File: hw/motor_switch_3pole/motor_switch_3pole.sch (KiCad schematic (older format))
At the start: 24 parts, among them J1 CONN_3X1, J2 CONN_2X1, J3 CONN_6X1, Q1 BSS138, Q2 BSS138

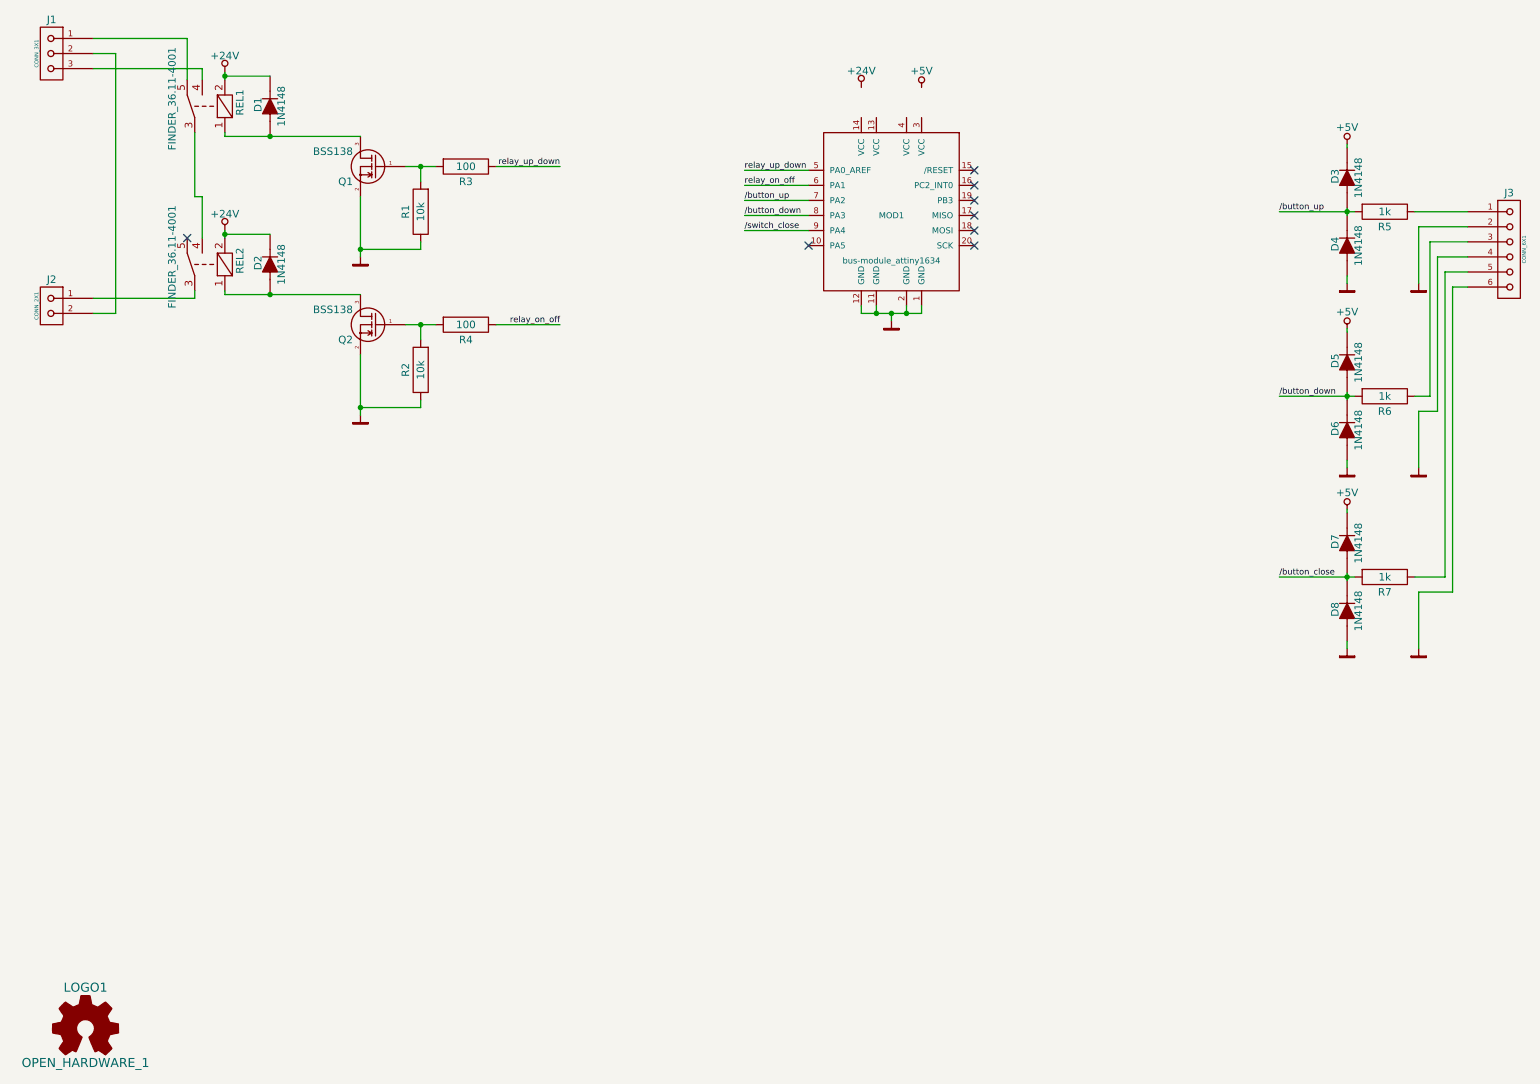
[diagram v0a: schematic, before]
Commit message: changed to SMD components
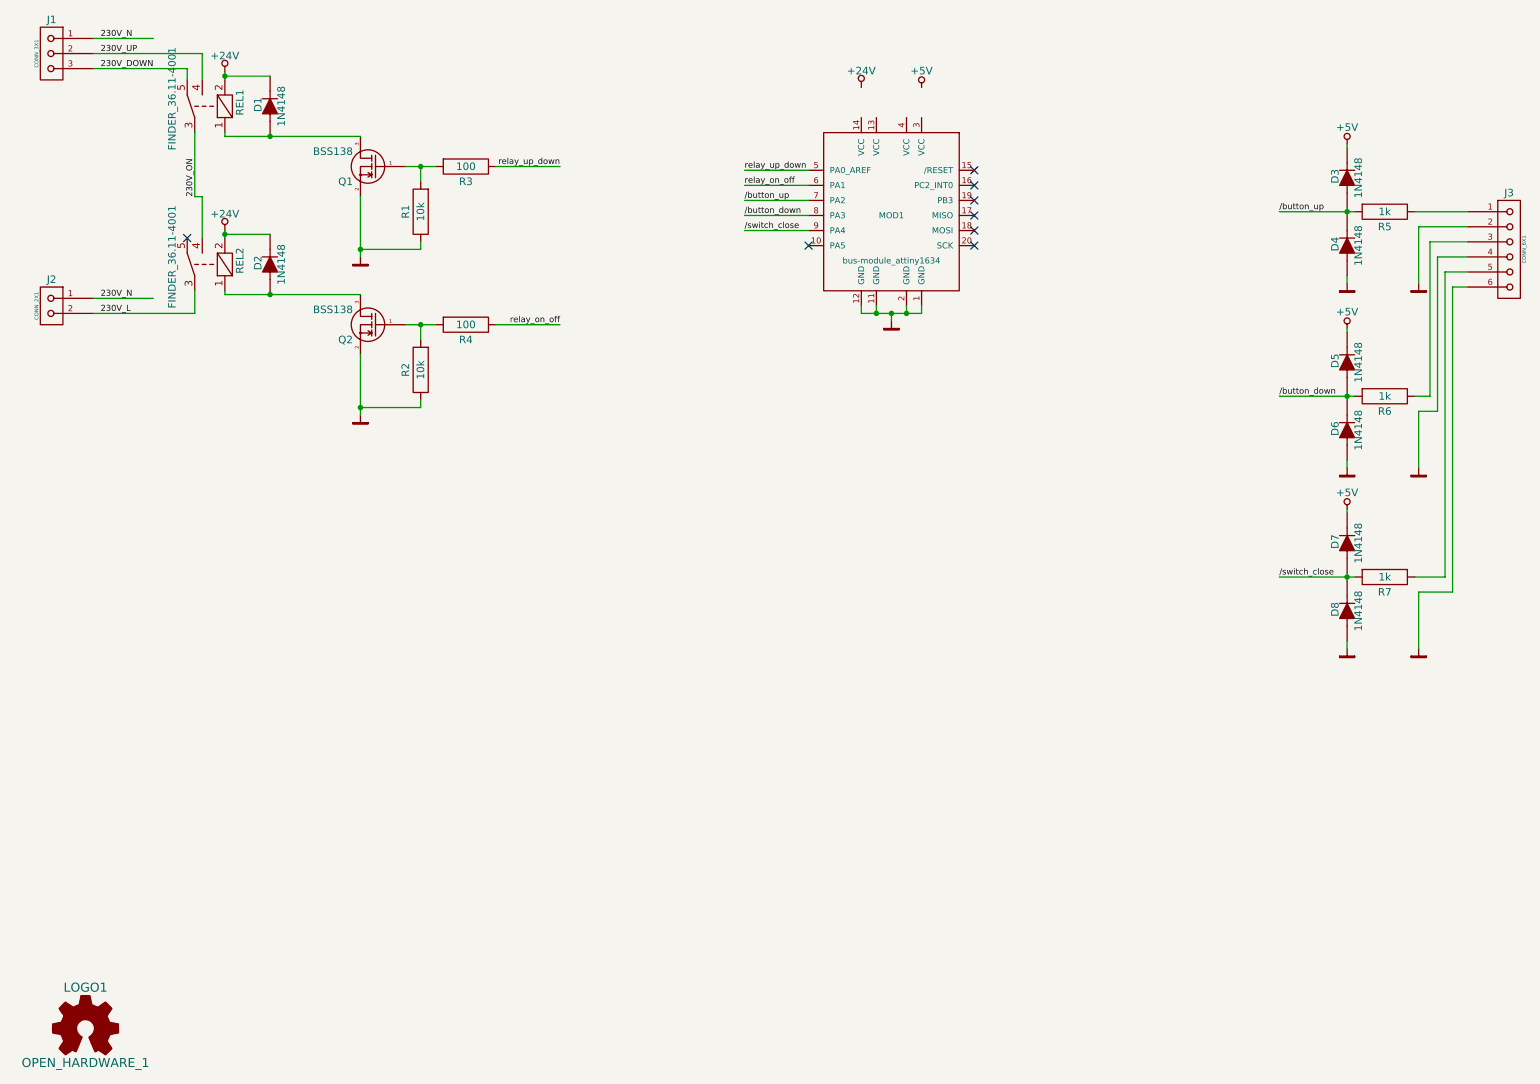
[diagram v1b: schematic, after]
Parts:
- D1, D2, D3, D4, D5, D6, D7, D8: footprint Diode_THT:D_RM2.54mm -> Diode_SMD:D_SOD323
- R1, R2, R3, R4, R5, R6, R7: footprint Resistor:R_RM2.54mm -> Resistor:R_0805
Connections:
- net /button_close is gone; now on net /switch_close: D7.1 (A), D8.2 (C), R7.1
- net 230V_ON: now reaches REL1.3, REL2.4
- net 230V_DOWN: now reaches J1.3
- net 230V_DOWN: now also REL1.5; no longer REL1.4
- net 230V_N: now reaches J1.1
- net 230V_N: now also J2.1; no longer REL1.5
- net 230V_L: now reaches REL2.3
- net 230V_L: now also J2.2; no longer J2.1
- net 230V_UP: now reaches J1.2
- net 230V_UP: now also REL1.4; no longer J2.2
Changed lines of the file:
@@
 F 0 "D1" H 2210 1305 50  0000 C CNN
 F 1 "1N4148" H 2200 1150 50  0000 C CNN
-F 2 "Diode_THT:D_RM2.54mm" H 2200 1225 60  0001 C CNN
+F 2 "Diode_SMD:D_SOD323" H 2200 1225 60  0001 C CNN
 F 3 "" H 2200 1225 60  0000 C CNN
 	1    2200 1225
@@
 F 0 "D2" H 2210 2355 50  0000 C CNN
 F 1 "1N4148" H 2200 2200 50  0000 C CNN
-F 2 "Diode_THT:D_RM2.54mm" H 2200 2275 60  0001 C CNN
+F 2 "Diode_SMD:D_SOD323" H 2200 2275 60  0001 C CNN
 F 3 "" H 2200 2275 60  0000 C CNN
 	1    2200 2275
@@
 F 0 "R3" H 3500 1525 50  0000 C CNN
 F 1 "100" H 3500 1625 50  0000 C CNN
-F 2 "Resistor:R_RM2.54mm" H 3500 1625 60  0001 C CNN
+F 2 "Resistor:R_0805" H 3500 1625 60  0001 C CNN
 F 3 "" H 3500 1625 60  0000 C CNN
 	1    3500 1625
@@
 F 0 "R1" H 3200 1825 50  0000 C CNN
 F 1 "10k" H 3200 1925 50  0000 C CNN
-F 2 "Resistor:R_RM2.54mm" H 3200 1925 60  0001 C CNN
+F 2 "Resistor:R_0805" H 3200 1925 60  0001 C CNN
 F 3 "" H 3200 1925 60  0000 C CNN
 	1    3200 1925
@@
 F 0 "R2" H 3200 2875 50  0000 C CNN
 F 1 "10k" H 3200 2975 50  0000 C CNN
-F 2 "Resistor:R_RM2.54mm" H 3200 2975 60  0001 C CNN
+F 2 "Resistor:R_0805" H 3200 2975 60  0001 C CNN
 F 3 "" H 3200 2975 60  0000 C CNN
 	1    3200 2975
@@
 F 0 "R4" H 3500 2575 50  0000 C CNN
 F 1 "100" H 3500 2675 50  0000 C CNN
-F 2 "Resistor:R_RM2.54mm" H 3500 2675 60  0001 C CNN
+F 2 "Resistor:R_0805" H 3500 2675 60  0001 C CNN
 F 3 "" H 3500 2675 60  0000 C CNN
 	1    3500 2675
@@
 	1900 2475 1900 2450
 Wire Wire Line
-	1025 875  1175 875
-Wire Wire Line
-	1175 2600 1025 2600
-Wire Wire Line
-	1025 2500 1700 2500
-Wire Wire Line
-	1700 2500 1700 2450
-Wire Wire Line
-	1650 1050 1650 775
-Wire Wire Line
-	1650 775  1025 775
-Wire Wire Line
-	1750 1050 1750 975
-Wire Wire Line
-	1750 975  1025 975
-Wire Wire Line
 	2800 2225 2800 1825
 Connection ~ 2200 1425
@@
 	3200 2175 2800 2175
 Connection ~ 2800 2175
-Wire Wire Line
-	1175 875  1175 2600
 Wire Wire Line
 	1750 2100 1750 1825
@@
 F 0 "D3" H 9360 1780 50  0000 C CNN
 F 1 "1N4148" H 9350 1625 50  0000 C CNN
-F 2 "Diode_THT:D_RM2.54mm" H 9350 1700 60  0001 C CNN
+F 2 "Diode_SMD:D_SOD323" H 9350 1700 60  0001 C CNN
 F 3 "" H 9350 1700 60  0000 C CNN
 	1    9350 1700
@@
 F 0 "D4" H 9360 2230 50  0000 C CNN
 F 1 "1N4148" H 9350 2075 50  0000 C CNN
-F 2 "Diode_THT:D_RM2.54mm" H 9350 2150 60  0001 C CNN
+F 2 "Diode_SMD:D_SOD323" H 9350 2150 60  0001 C CNN
 F 3 "" H 9350 2150 60  0000 C CNN
 	1    9350 2150
@@
 F 0 "R5" H 9600 1825 50  0000 C CNN
 F 1 "1k" H 9600 1925 50  0000 C CNN
-F 2 "Resistor:R_RM2.54mm" H 9600 1925 60  0001 C CNN
+F 2 "Resistor:R_0805" H 9600 1925 60  0001 C CNN
 F 3 "" H 9600 1925 60  0000 C CNN
 	1    9600 1925
@@
 F 0 "D5" H 9360 3005 50  0000 C CNN
 F 1 "1N4148" H 9350 2850 50  0000 C CNN
-F 2 "Diode_THT:D_RM2.54mm" H 9350 2925 60  0001 C CNN
+F 2 "Diode_SMD:D_SOD323" H 9350 2925 60  0001 C CNN
 F 3 "" H 9350 2925 60  0000 C CNN
 	1    9350 2925
@@
 F 0 "D6" H 9360 3455 50  0000 C CNN
 F 1 "1N4148" H 9350 3300 50  0000 C CNN
-F 2 "Diode_THT:D_RM2.54mm" H 9350 3375 60  0001 C CNN
+F 2 "Diode_SMD:D_SOD323" H 9350 3375 60  0001 C CNN
 F 3 "" H 9350 3375 60  0000 C CNN
 	1    9350 3375
@@
 F 0 "R6" H 9600 3050 50  0000 C CNN
 F 1 "1k" H 9600 3150 50  0000 C CNN
-F 2 "Resistor:R_RM2.54mm" H 9600 3150 60  0001 C CNN
+F 2 "Resistor:R_0805" H 9600 3150 60  0001 C CNN
 F 3 "" H 9600 3150 60  0000 C CNN
 	1    9600 3150
@@
 F 0 "D7" H 9360 4205 50  0000 C CNN
 F 1 "1N4148" H 9350 4050 50  0000 C CNN
-F 2 "Diode_THT:D_RM2.54mm" H 9350 4125 60  0001 C CNN
+F 2 "Diode_SMD:D_SOD323" H 9350 4125 60  0001 C CNN
 F 3 "" H 9350 4125 60  0000 C CNN
 	1    9350 4125
@@
 F 0 "D8" H 9360 4655 50  0000 C CNN
 F 1 "1N4148" H 9350 4500 50  0000 C CNN
-F 2 "Diode_THT:D_RM2.54mm" H 9350 4575 60  0001 C CNN
+F 2 "Diode_SMD:D_SOD323" H 9350 4575 60  0001 C CNN
 F 3 "" H 9350 4575 60  0000 C CNN
 	1    9350 4575
@@
 F 0 "R7" H 9600 4250 50  0000 C CNN
 F 1 "1k" H 9600 4350 50  0000 C CNN
-F 2 "Resistor:R_RM2.54mm" H 9600 4350 60  0001 C CNN
+F 2 "Resistor:R_0805" H 9600 4350 60  0001 C CNN
 F 3 "" H 9600 4350 60  0000 C CNN
 	1    9600 4350
@@
 Connection ~ 9350 4350
 Text Label 8900 4350 0    40   ~ 0
-/button_close
+/switch_close
 $Comp
 L +5V #PWR012
@@
 	-1   0    0    -1
 $EndComp
+Text Label 1075 875  0    40   ~ 0
+230V_UP
+Text Label 1075 975  0    40   ~ 0
+230V_DOWN
+Text Label 1700 1825 1    40   ~ 0
+230V_ON
+Text Label 1075 775  0    40   ~ 0
+230V_N
+Text Label 1075 2600 0    40   ~ 0
+230V_L
+Wire Wire Line
+	1650 1050 1650 975
+Wire Wire Line
+	1650 975  1025 975
+Wire Wire Line
+	1025 875  1750 875
+Wire Wire Line
+	1750 875  1750 1050
+Wire Wire Line
+	1025 2600 1700 2600
+Wire Wire Line
+	1700 2600 1700 2450
+Wire Wire Line
+	1025 2500 1425 2500
+Wire Wire Line
+	1025 775  1425 775
+Text Label 1075 2500 0    40   ~ 0
+230V_N
 $EndSCHEMATC

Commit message: motor control 3pole layouted and ready for review
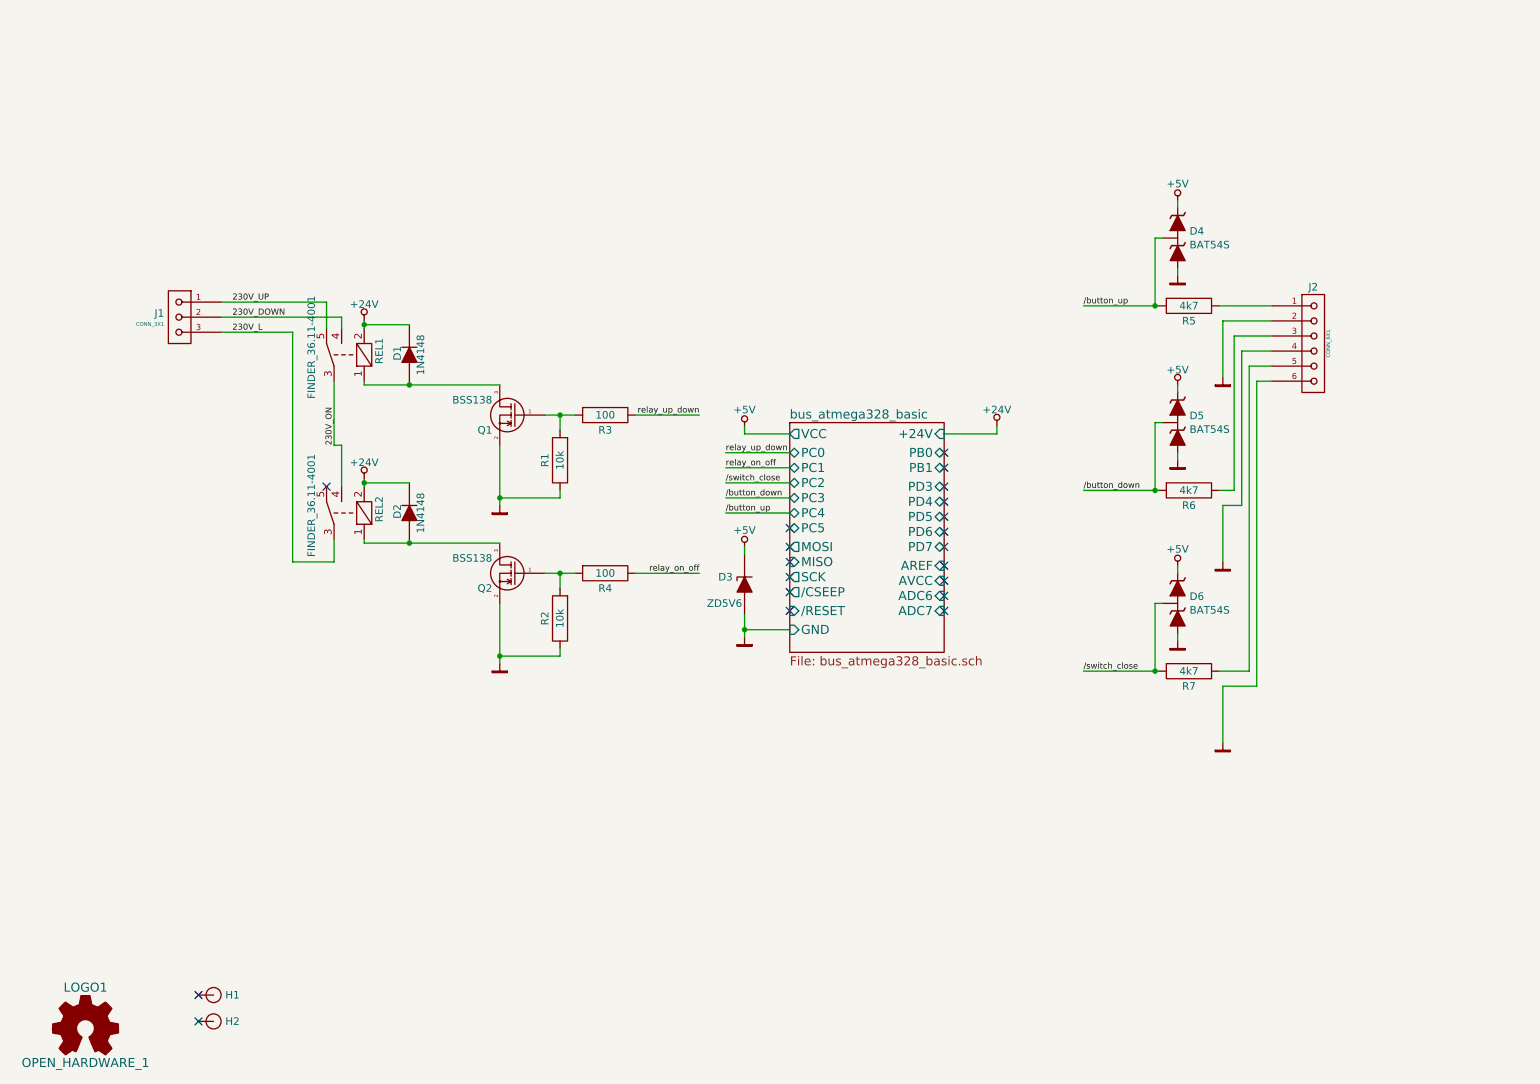
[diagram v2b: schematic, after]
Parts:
- removed D3, D4, D5, D6, D7, D8: 1N4148, Diode_SMD:D_SOD323, symbol D
- removed J2: CONN_2X1, Connector_Miscelleaneus:CLAMP_5,08mm_2pole_stackable, symbol CONN_2X1
- removed MOD1: bus-module_attiny1634, Modules:bus-module_attiny1634, symbol bus-module_attiny1634
- added D3: ZD5V6, Diode_SMD:D_MINIMELF, symbol ZD
- added D4, D5, D6: BAT54S, Housings_SOT:SOT23-3, symbol BAT54S
- added H1, H2: HOLE, Mechanical:HOLE_2.5mm_wo_Copper, symbol HOLE
- J1: footprint Connector_Miscelleaneus:CLAMP_5,08mm_3pole_stackable -> Connector_WAGO:WAGO_2081-1123
- J2: renamed from J3; footprint Connector_Miscelleaneus:WAGO_233-6 -> Connector_WAGO:WAGO_233-6
- R5, R6, R7: value 1k -> 4k7
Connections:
- net 230V_N is gone; now on net 230V_UP: J1.1
- net +5V: now also D3.2 (C), D4.2, D5.2, D6.2
- net /button_down: now also D5.3
- net /button_up: now also D4.3
- net /switch_close: now also D6.3
- net 230V_DOWN: now also J1.2, REL1.4; no longer J1.3, REL1.5
- net 230V_L: now also J1.3
- net 230V_UP: now also REL1.5; no longer J1.2, REL1.4
- net GND: now also D3.1 (A), D4.1, D5.1, D6.1
- no-connect marks 8 -> 20
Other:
- moved on the sheet: D1, D2, J2, Q1, Q2, R1, R2, R3, R4, R5, R6, R7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

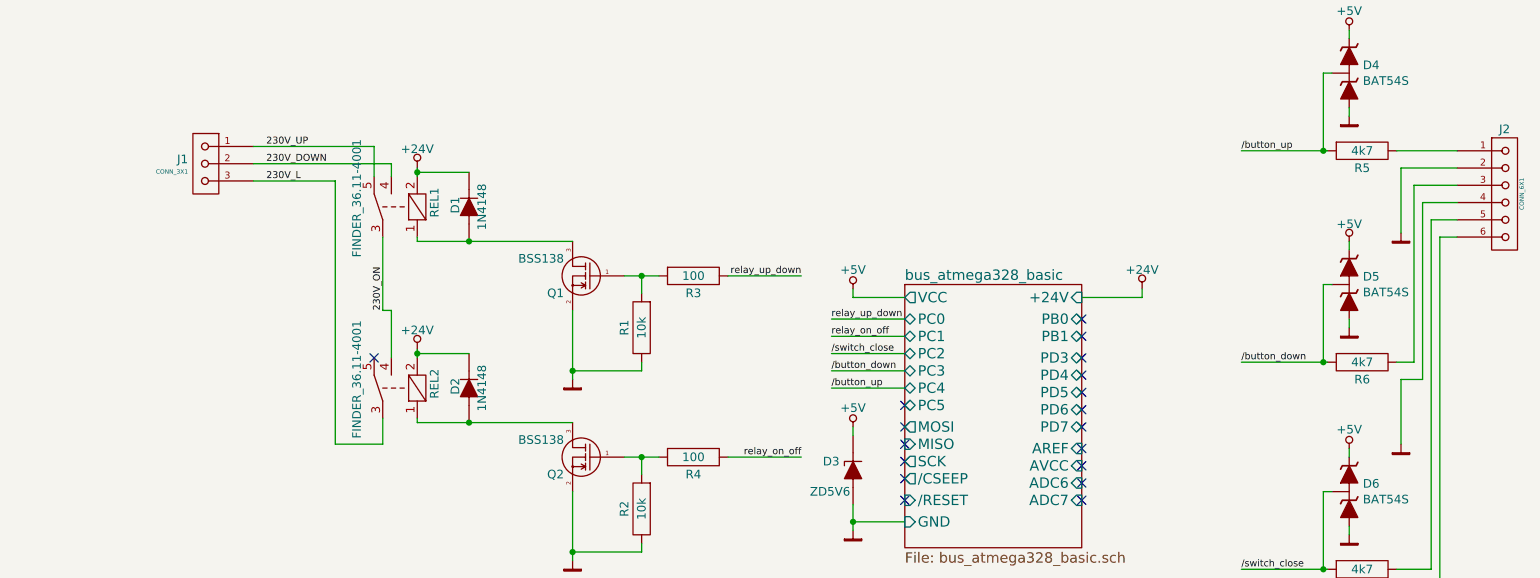
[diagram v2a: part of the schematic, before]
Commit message: Final revision 1 files of motor_switch_3pole added. Prototype PCBs of this revision have been ordered
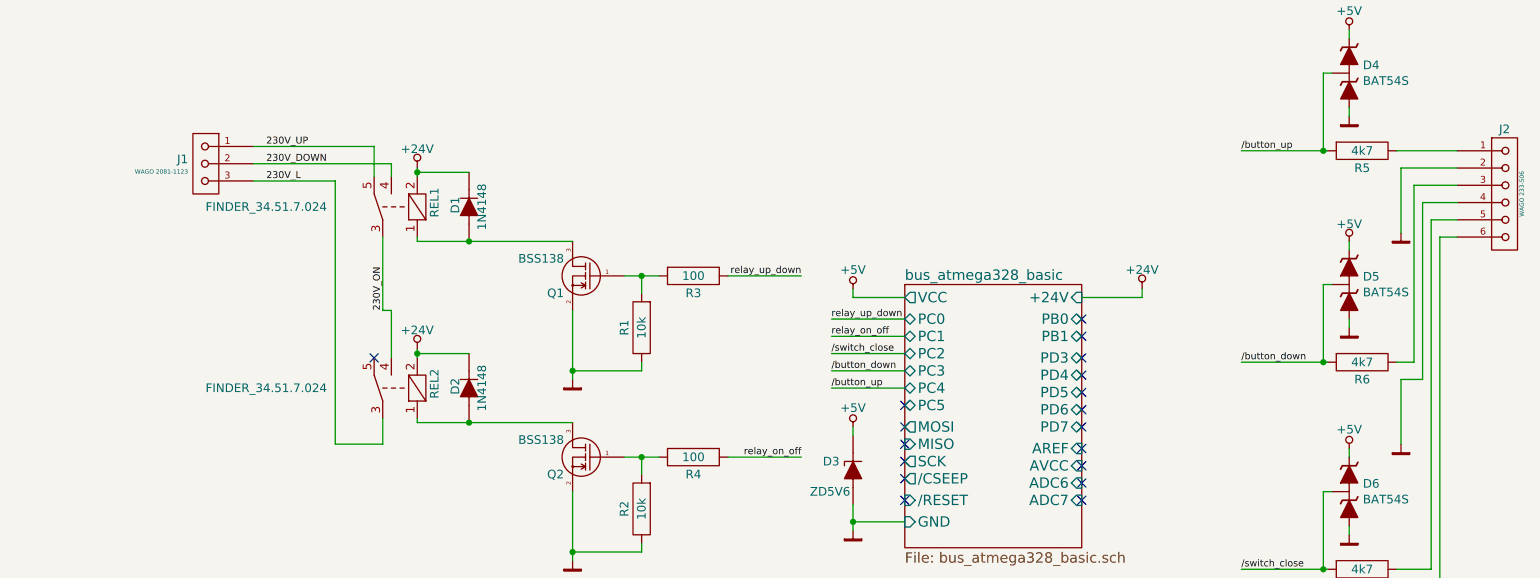
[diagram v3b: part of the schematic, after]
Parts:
- J1: value CONN_3X1 -> WAGO 2081-1123
- J2: value CONN_6X1 -> WAGO 233-506
- REL1, REL2: value FINDER_36.11-4001 -> FINDER_34.51.7.024
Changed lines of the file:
@@
 Sheet 1 2
 Title "motor switch 3pole"
-Date "2016-08-10"
+Date "2016-09-06"
 Rev "1"
 Comp "koewiba"
@@
 P 2825 2875
 F 0 "REL1" H 2850 2775 50  0000 C CNN
-F 1 "FINDER_36.11-4001" H 2875 3225 50  0000 C CNN
+F 1 "FINDER_34.51.7.024" V 2825 3750 50  0000 C CNN
 F 2 "Relay:finder_34.51_1xUM" H 2825 2875 60  0001 C CNN
 F 3 "" H 2825 2875 60  0000 C CNN
@@
 P 2825 3925
 F 0 "REL2" H 2850 3825 50  0000 C CNN
-F 1 "FINDER_36.11-4001" H 2875 4275 50  0000 C CNN
+F 1 "FINDER_34.51.7.024" V 2825 4800 50  0000 C CNN
 F 2 "Relay:finder_34.51_1xUM" H 2825 3925 60  0001 C CNN
 F 3 "" H 2825 3925 60  0000 C CNN
@@
 P 9050 2800
 F 0 "J2" H 9125 3175 50  0000 C CNN
-F 1 "CONN_6X1" V 9225 2800 25  0000 C CNN
+F 1 "WAGO 233-506" V 9225 2800 25  0000 C CNN
 F 2 "Connector_WAGO:WAGO_233-6" H 9050 2800 60  0001 C CNN
 F 3 "" H 9050 2800 60  0000 C CNN
@@
 P 1675 2625
 F 0 "J1" H 1853 2651 50  0000 L CNN
-F 1 "CONN_3X1" H 1853 2579 25  0000 L CNN
+F 1 "WAGO 2081-1123" H 1853 2579 25  0000 L CNN
 F 2 "Connector_WAGO:WAGO_2081-1123" H 1675 2625 60  0001 C CNN
 F 3 "" H 1675 2625 60  0000 C CNN
